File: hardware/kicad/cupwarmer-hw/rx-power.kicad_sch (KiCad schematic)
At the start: 41 parts, among them J1 I2C Service, J3 STATUS_MON, U1 STWLC38JRM

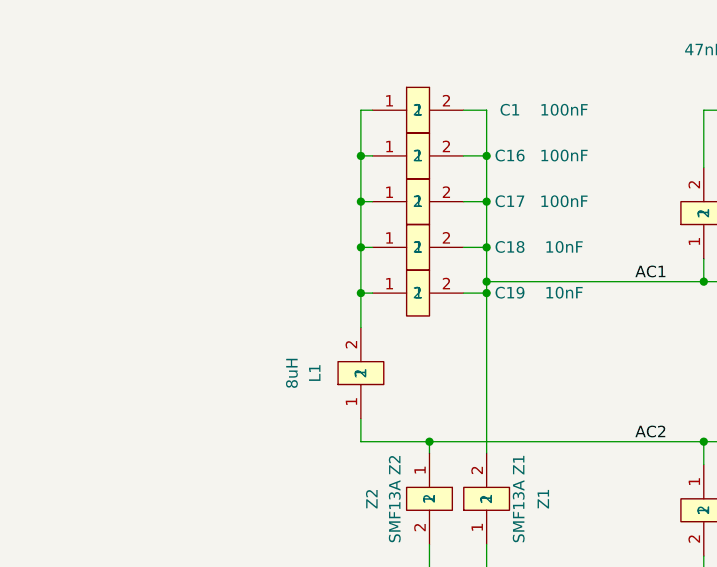
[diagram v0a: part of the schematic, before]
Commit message: Assign netclasses and unblock U1 routing
- kicad_pro: assign POWER (VOUT_12V, VRECT, RX_VAA, RX_VDD, SYS_GND,
  AC1, AC2) and SENSE (BOOT1/2, COMA1/2, COMB1/2); add 0.2mm to
  pre-defined track widths
- pcb: U1 local pad clearance override 0.13mm so 0.4mm-pitch WLCSP
  pads stop reporting clearance violations against each other; add
  initial AC1/VRECT/SYS_GND track segments
- rx-power.sch: label coil-side AC1 net ("AC1 COIL")

Co-Authored-By: Claude Opus 4.7 (1M context) <noreply@anthropic.com>
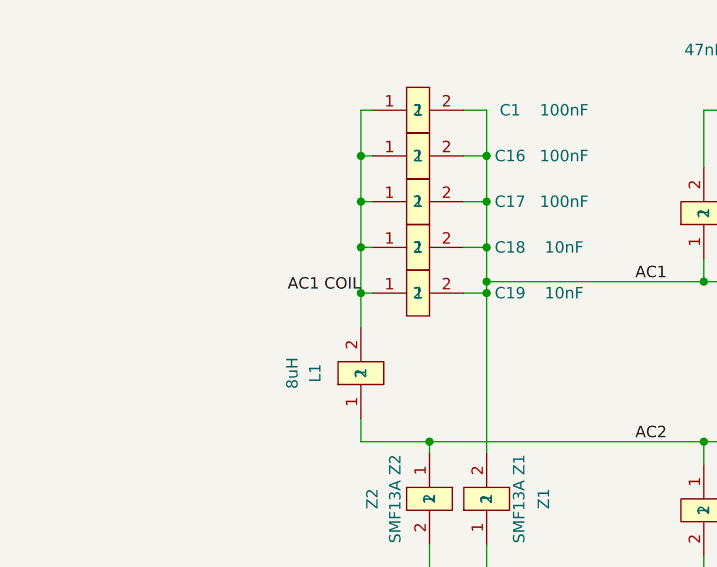
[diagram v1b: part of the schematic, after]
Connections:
- net AC1 COIL: now reaches C1.1, C16.1, C17.1, C18.1, C19.1, L1.2
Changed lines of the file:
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@@
+		)
+	)
+	(label "AC1 COIL"
+		(at 58.42 96.52 180)
+		(effects
+			(font
+				(size 1.27 1.27)
+			)
+			(justify right bottom)
 		)
 	)

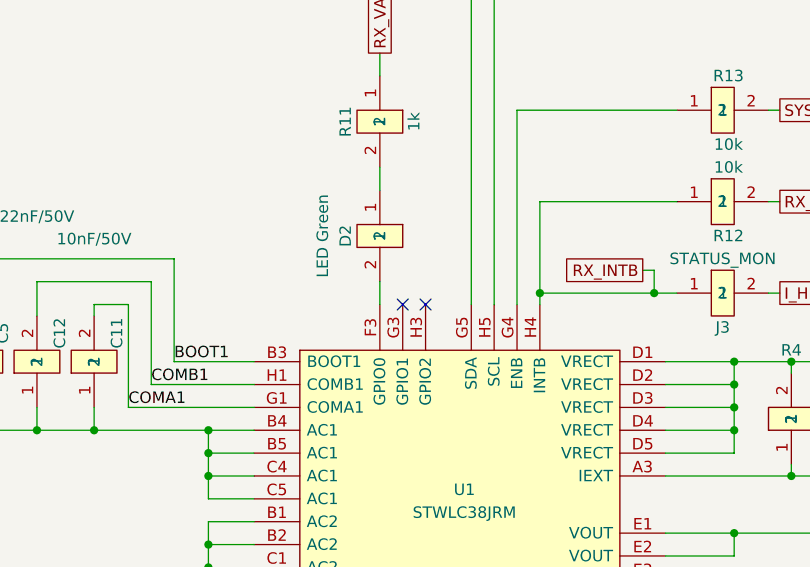
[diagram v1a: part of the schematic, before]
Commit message: Route U1 area and tighten board design rules
Reposition rx-power footprints around U1, add LED2 label on
rx-power.kicad_sch, drop min_hole_clearance to 0.1mm, add a 0.13/0.1mm
via size and a 0.1mm track width, and add a custom DRU rule allowing
zero clearance inside U1's courtyard so dense routing under the IC
passes DRC.

Co-Authored-By: Claude Opus 4.7 (1M context) <noreply@anthropic.com>
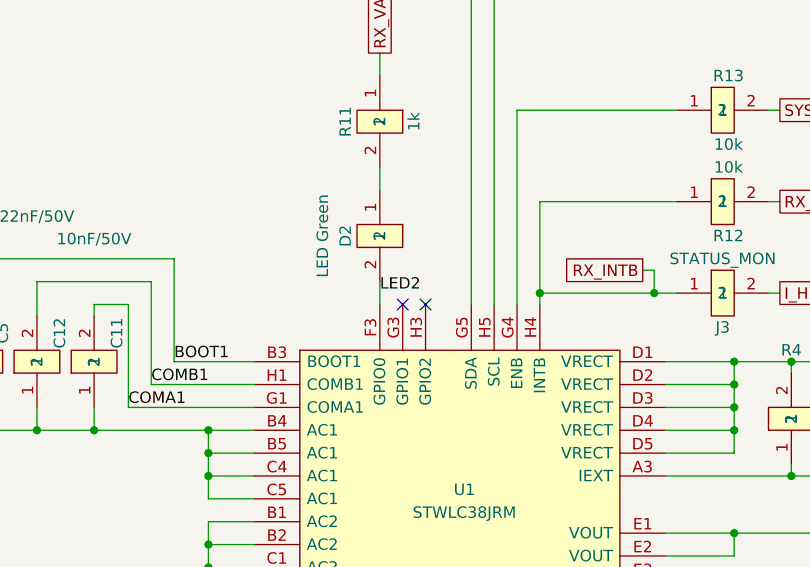
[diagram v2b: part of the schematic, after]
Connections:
- net LED2: now reaches D2.2, U1.F3 (GPIO0)
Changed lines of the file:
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@@
+		)
+	)
+	(label "LED2"
+		(at 140.97 80.01 0)
+		(effects
+			(font
+				(size 1.27 1.27)
+			)
+			(justify left bottom)
 		)
 	)
